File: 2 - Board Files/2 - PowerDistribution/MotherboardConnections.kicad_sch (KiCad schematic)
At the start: 0 parts

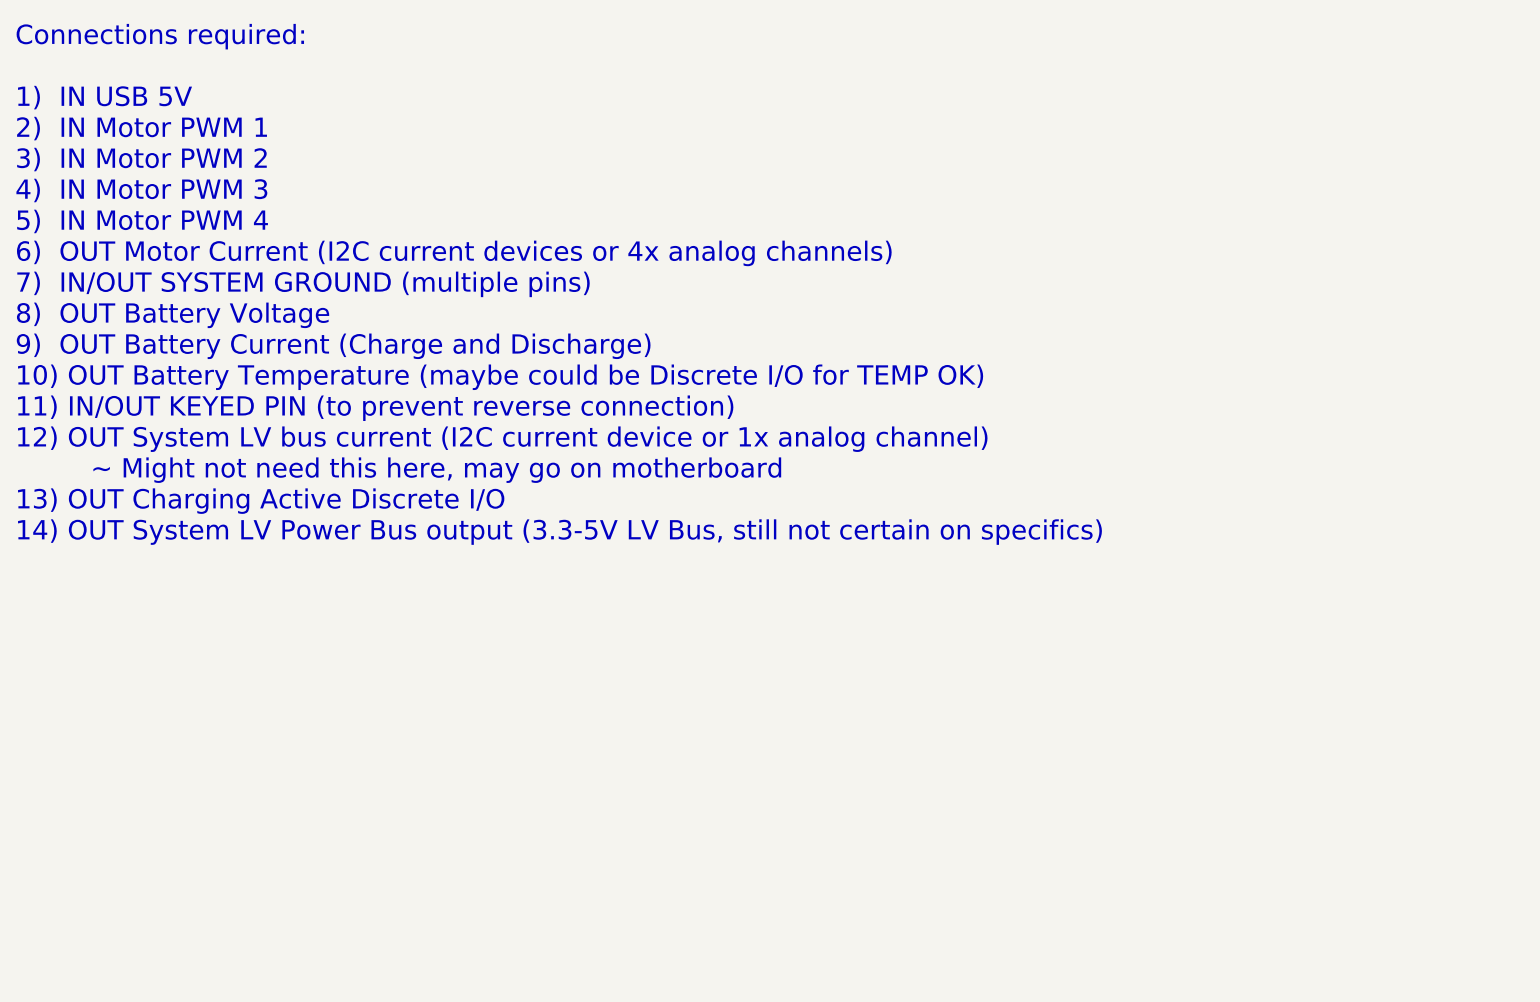
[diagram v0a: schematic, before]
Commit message: Added sch and pcb for initial power input stage
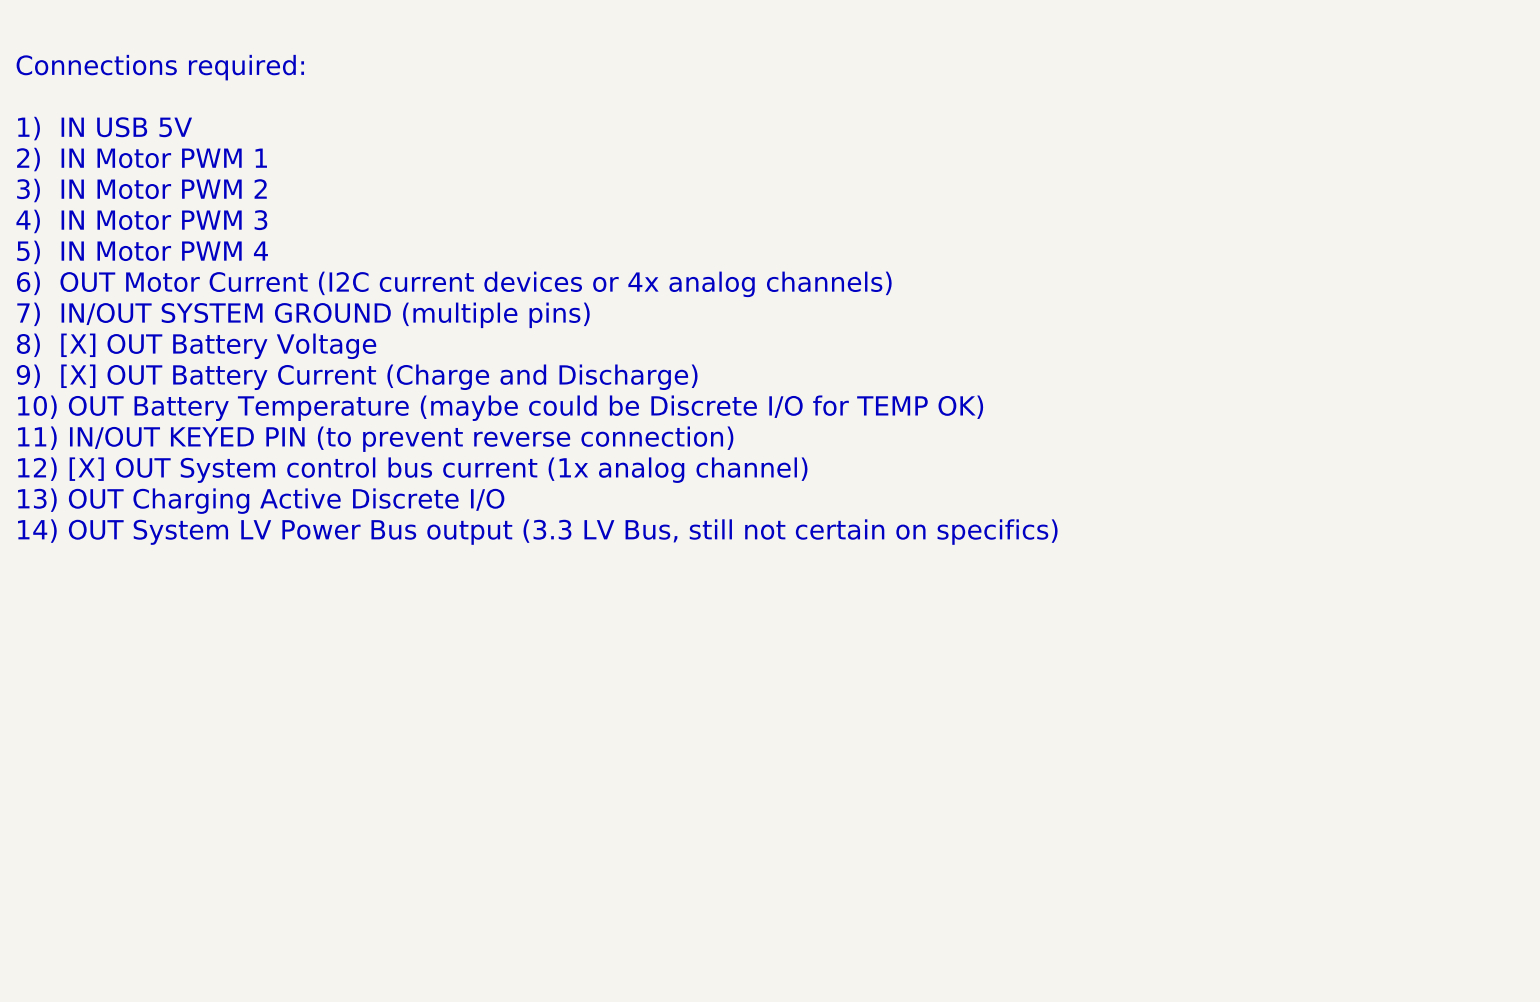
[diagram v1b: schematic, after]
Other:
- note added: "Connections required: 1) IN USB 5V 2) IN Motor PWM 1 3) IN Motor PWM 2 4) IN Motor PWM 3 5) IN Motor PWM 4 6) OUT Motor Current (I2C current devices or 4x analog channels) 7) IN/OUT SYSTEM GROUND (multiple pins) 8) [X] OUT Battery Voltage 9) [X] OUT Battery Current (Charge and Discharge) 10) OUT Battery Temperature (maybe could be Discrete I/O for TEMP OK) 11) IN/OUT KEYED PIN (to prevent reverse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"
- note removed: "Connections required: 1) IN USB 5V 2) IN Motor PWM 1 3) IN Motor PWM 2 4) IN Motor PWM 3 5) IN Motor PWM 4 6) OUT Motor Current (I2C current devices or 4x analog channels) 7) IN/OUT SYSTEM GROUND (multiple pins) 8) OUT Battery Voltage 9) OUT Battery Current (Charge and Discharge) 10) OUT Battery Temperature (maybe could be Discrete I/O for TEMP OK) 11) IN/OUT KEYED PIN (to prevent reverse connect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"
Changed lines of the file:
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@@
 (kicad_sch (version 20211123) (generator eeschema)
   (paper "A4")
-  (text "Connections required:\n\n1)  IN USB 5V\n2)  IN Motor PWM 1\n3)  IN Motor PWM 2\n4)  IN Motor PWM 3\n5)  IN Motor PWM 4\n6)  OUT Motor Current (I2C current devices or 4x analog channels)\n7)  IN/OUT SYSTEM GROUND (multiple pins)\n8)  OUT Battery Voltage\n9)  OUT Battery Current (Charge and Discharge)\n10) OUT Battery Temperature (maybe could be Discrete I/O for TEMP OK)\n11) IN/OUT KEYED PIN (to prevent reverse connection)\n12) OUT System LV bus current (I2C current device or 1x analog channel)\n         ~ Might not need this here, may go on motherboard\n13) OUT Charging Active Discrete I/O\n14) OUT System LV Power Bus output (3.3-5V LV Bus, still not certain on specifics)"
+  (text "Connections required:\n\n1)  IN USB 5V\n2)  IN Motor PWM 1\n3)  IN Motor PWM 2\n4)  IN Motor PWM 3\n5)  IN Motor PWM 4\n6)  OUT Motor Current (I2C current devices or 4x analog channels)\n7)  IN/OUT SYSTEM GROUND (multiple pins)\n8)  [X] OUT Battery Voltage\n9)  [X] OUT Battery Current (Charge and Discharge)\n10) OUT Battery Temperature (maybe could be Discrete I/O for TEMP OK)\n11) IN/OUT KEYED PIN (to prevent reverse connection)\n12) [X] OUT System control bus current (1x analog channel)\n13) OUT Charging Active Discrete I/O\n14) OUT System LV Power Bus output (3.3 LV Bus, still not certain on specifics)"
     (at 19.05 90.17 0)
     (effects (font (size 2.54 2.54)) (justify left bottom))

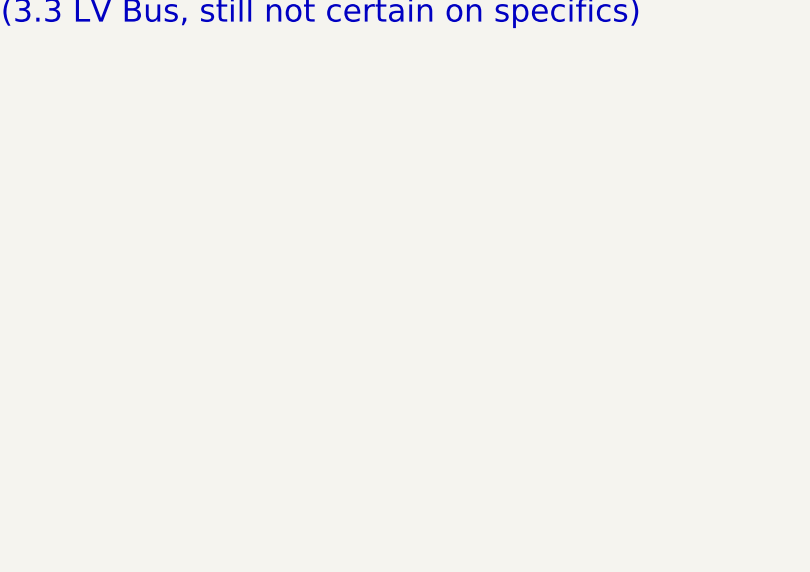
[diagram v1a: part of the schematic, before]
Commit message: Part values for power input stage
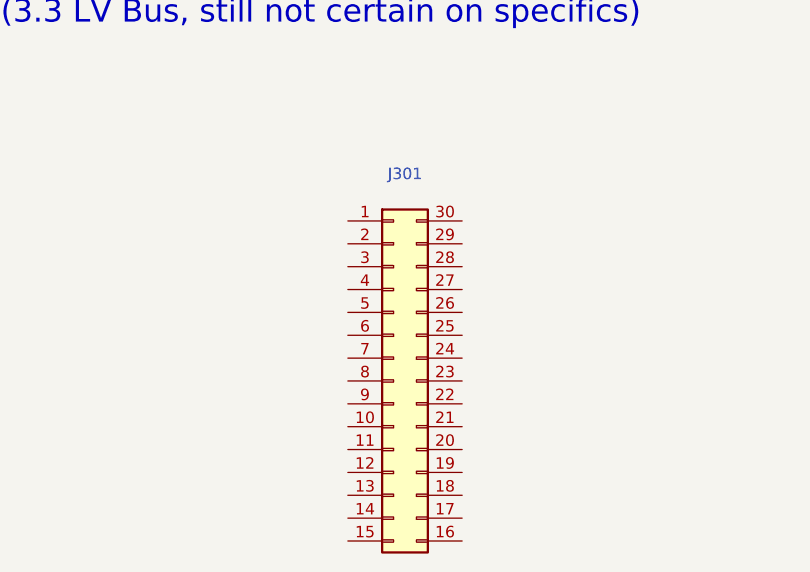
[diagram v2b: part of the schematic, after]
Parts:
- added J301: Conn_02x15_Counter_Clockwise, Connector_PinHeader_1.27mm:PinHeader_2x15_P1.27mm_Vertical_SMD, symbol Connector_Generic:Conn_02x15_Counter_Clockwise
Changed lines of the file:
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@@
     (effects (font (size 2.54 2.54)) (justify left bottom))
   )
+  (symbol (lib_id "Connector_Generic:Conn_02x15_Counter_Clockwise") (at 129.54 129.54 0) (unit 1)
+    (in_bom yes) (on_board yes) (fields_autoplaced)
+    (property "Reference" "J301" (id 0) (at 130.81 106.5235 0))
+    (property "Value" "Conn_02x15_Counter_Clockwise" (id 1) (at 130.81 109.2986 0)
+      (effects (font (size 1.27 1.27)) hide)
+    )
+    (property "Footprint" "Connector_PinHeader_1.27mm:PinHeader_2x15_P1.27mm_Vertical_SMD" (id 2) (at 129.54 129.54 0)
+      (effects (font (size 1.27 1.27)) hide)
+    )
+    (property "Datasheet" "~" (id 3) (at 129.54 129.54 0)
+      (effects (font (size 1.27 1.27)) hide)
+    )
+    (pin "1")
+    (pin "10")
+    (pin "11")
+    (pin "12")
+    (pin "13")
+    (pin "14")
+    (pin "15")
+    (pin "16")
+    (pin "17")
+    (pin "18")
+    (pin "19")
+    (pin "2")
+    (pin "20")
+    (pin "21")
+    (pin "22")
+    (pin "23")
+    (pin "24")
+    (pin "25")
+    (pin "26")
+    (pin "27")
+    (pin "28")
+    (pin "29")
+    (pin "3")
+    (pin "30")
+    (pin "4")
+    (pin "5")
+    (pin "6")
+    (pin "7")
+    (pin "8")
+    (pin "9")
+  )
 )
